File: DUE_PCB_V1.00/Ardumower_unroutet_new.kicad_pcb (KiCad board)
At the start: 2 copper layers, 169.8 x 97 mm, 86 parts, among them J1 9V IN, J10 Sonar_R, J11 Sonar_C, J12 Sonar_L, J13 P_Right, J14 Buzzer, J15 Button, J16 US1, J17 US2, J18 US3, J19 P_Left, J2 I2C0_1, J20 Remote, J21 PCB_2, J22 Ser0, J23 Ser1, J24 Ser2, J25 5V IN, J26 Cutter1, J27 MotorR, J28 MotorL, J29 3.3V IN, J3 I2C0_2, J30 I2C1_2, J31 Ser3, J32 24V In, J33 ReserveD8, J34 ReserveD9, J35 ReserveD49, J36 ReserveA10, J37 RPM_Mow, J38 ODO_Left, J39 ODO_Right, J4 I2C1_1, J40 Motor_Right, J41 Motor_Left, J42 Cutter, J5 Bumper, J6 Drop_Left, J7 Drop_Right, J8 Tilt, J9 Rain, U1 MC33926, U2 MC33926

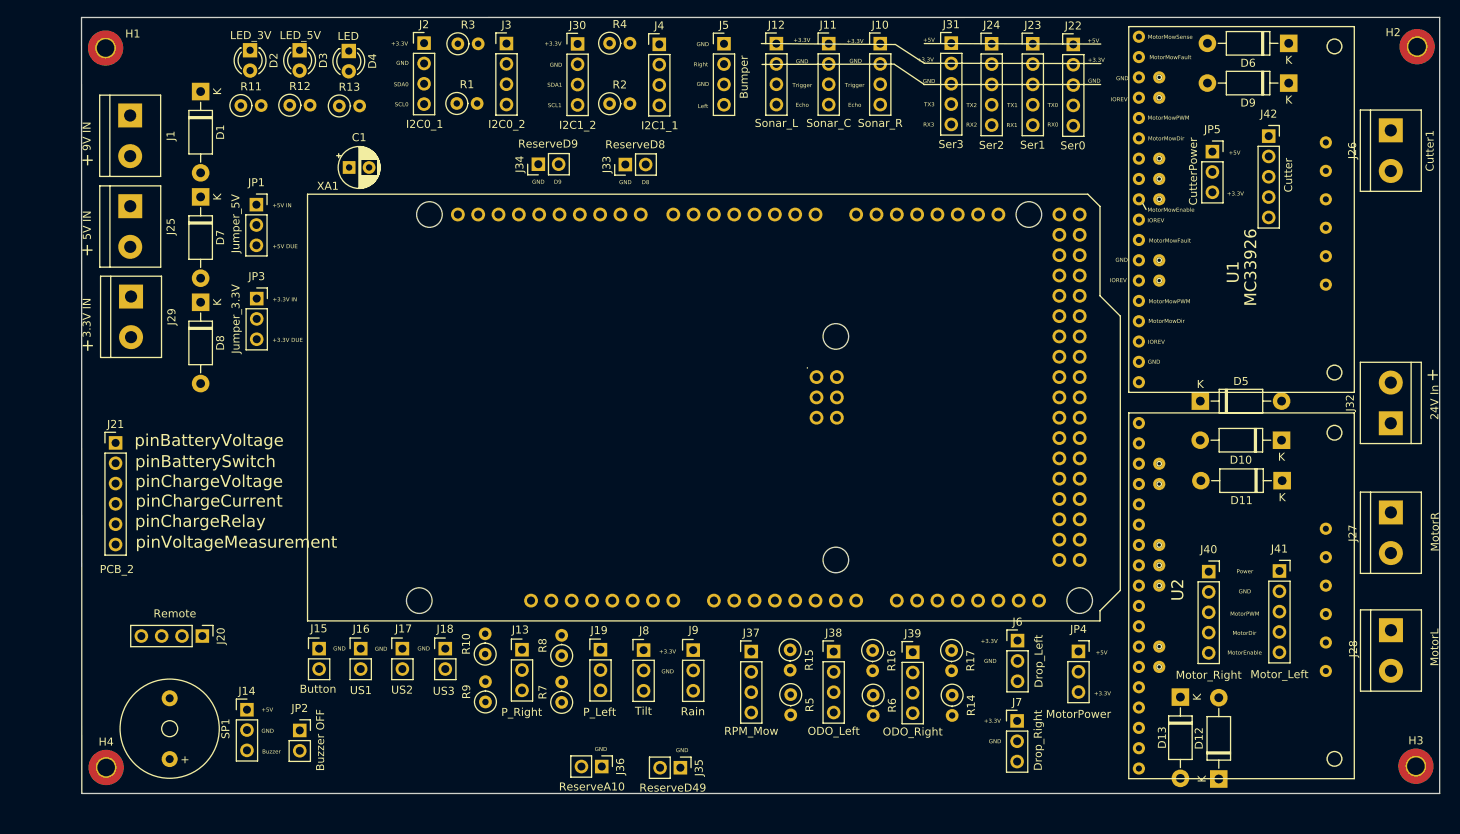
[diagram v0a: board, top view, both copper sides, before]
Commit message: Board Route
Board routed and make Gerber Files
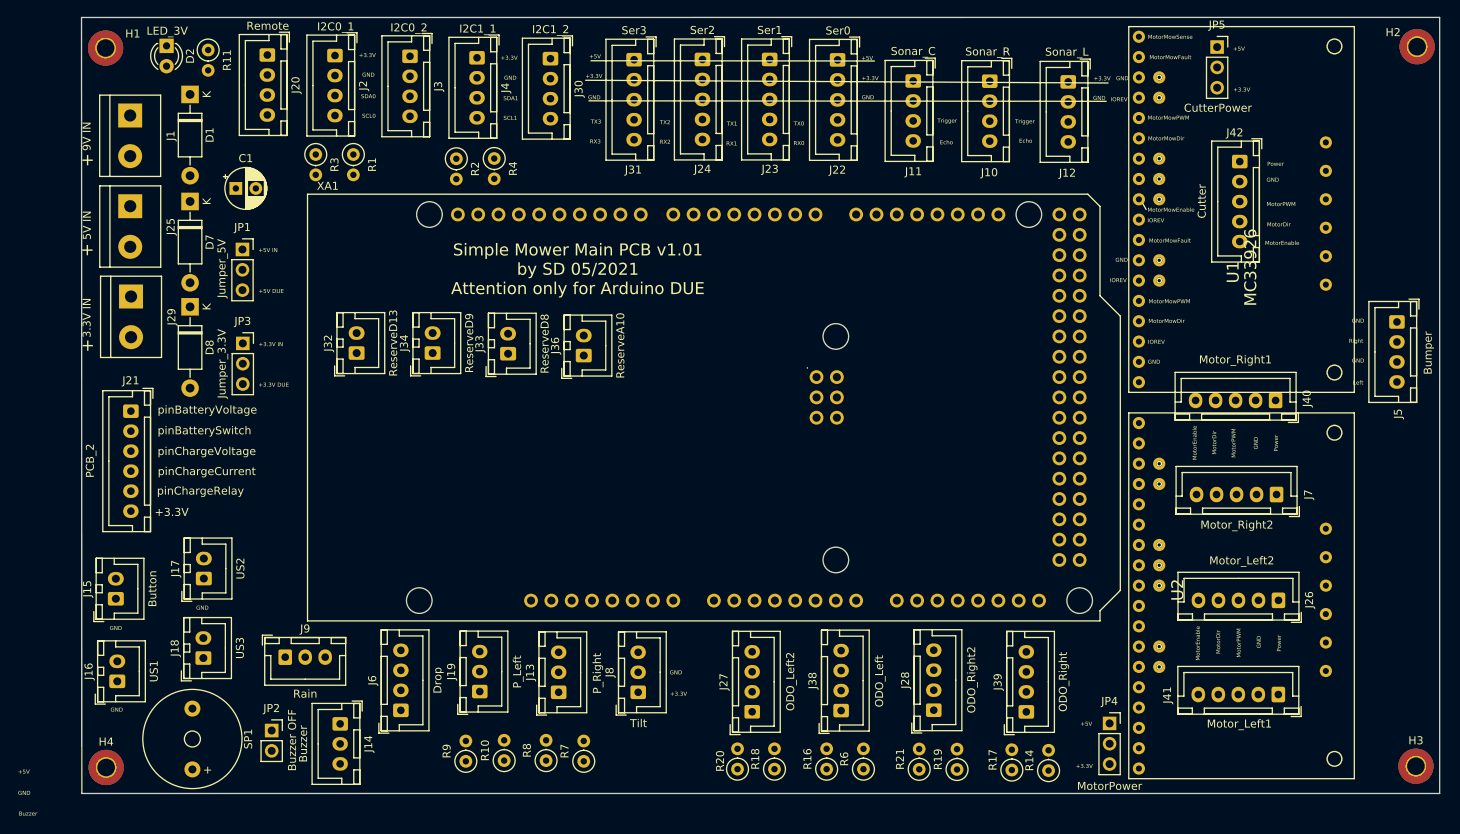
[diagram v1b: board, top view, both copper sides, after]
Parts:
- removed D10, D11, D12, D13, D5, D6, D9: 1N4728A, Diode_THT:D_DO-41_SOD81_P10.16mm_Horizontal
- removed D3: LED_5V, LED_THT:LED_D3.0mm
- removed D4: LED, LED_THT:LED_D3.0mm
- removed J35: ReserveD49, Connector_PinHeader_2.54mm:PinHeader_1x02_P2.54mm_Vertical
- removed J37: RPM_Mow, Connector_PinHeader_2.54mm:PinHeader_1x04_P2.54mm_Vertical
- removed R12: 220, Resistor_THT:R_Axial_DIN0207_L6.3mm_D2.5mm_P2.54mm_Vertical
- removed R13: 100, Resistor_THT:R_Axial_DIN0207_L6.3mm_D2.5mm_P2.54mm_Vertical
- removed R15: 1,5KO, Resistor_THT:R_Axial_DIN0207_L6.3mm_D2.5mm_P2.54mm_Vertical
- removed R5: 1KO, Resistor_THT:R_Axial_DIN0207_L6.3mm_D2.5mm_P2.54mm_Vertical
- added R18: 1KO, Resistor_THT:R_Axial_DIN0207_L6.3mm_D2.5mm_P2.54mm_Vertical, F.Cu at (125.4, 128.6)
- added R19: 1KO, Resistor_THT:R_Axial_DIN0207_L6.3mm_D2.5mm_P2.54mm_Vertical, F.Cu at (148.2, 128.6)
- added R20: 1,5KO, Resistor_THT:R_Axial_DIN0207_L6.3mm_D2.5mm_P2.54mm_Vertical, F.Cu at (120.8, 128.6)
- added R21: 1,5KO, Resistor_THT:R_Axial_DIN0207_L6.3mm_D2.5mm_P2.54mm_Vertical, F.Cu at (143.5, 128.6)
- J10, J11, J12, J2, J20, J3, J30, J38, J39, J4, J5: footprint Connector_PinHeader_2.54mm:PinHeader_1x04_P2.54mm_Vertical -> Connector_JST:JST_XH_B4B-XH-A_1x04_P2.50mm_Vertical
- J13, J14, J19, J8, J9: footprint Connector_PinHeader_2.54mm:PinHeader_1x03_P2.54mm_Vertical -> Connector_JST:JST_XH_B3B-XH-A_1x03_P2.50mm_Vertical
- J15, J16, J17, J18, J33, J34, J36: footprint Connector_PinHeader_2.54mm:PinHeader_1x02_P2.54mm_Vertical -> Connector_JST:JST_XH_B2B-XH-A_1x02_P2.50mm_Vertical
- J21: footprint Connector_PinHeader_2.54mm:PinHeader_1x06_P2.54mm_Vertical -> Connector_JST:JST_XH_B6B-XH-A_1x06_P2.50mm_Vertical
- J22, J23, J24, J31: footprint Connector_PinHeader_2.54mm:PinHeader_1x05_P2.54mm_Vertical -> Connector_JST:JST_XH_B5B-XH-A_1x05_P2.50mm_Vertical
- J26: value Cutter1 -> Motor_Left2; footprint TerminalBlock:TerminalBlock_bornier-2_P5.08mm -> Connector_JST:JST_XH_B5B-XH-A_1x05_P2.50mm_Vertical
- J27: value MotorR -> ODO_Left2; footprint TerminalBlock:TerminalBlock_bornier-2_P5.08mm -> Connector_JST:JST_XH_B4B-XH-A_1x04_P2.50mm_Vertical
- J28: value MotorL -> ODO_Right2; footprint TerminalBlock:TerminalBlock_bornier-2_P5.08mm -> Connector_JST:JST_XH_B4B-XH-A_1x04_P2.50mm_Vertical
- J32: value 24V In -> ReserveD13; footprint TerminalBlock:TerminalBlock_bornier-2_P5.08mm -> Connector_JST:JST_XH_B2B-XH-A_1x02_P2.50mm_Vertical
- J40: value Motor_Right -> Motor_Right1; footprint Connector_PinSocket_2.54mm:PinSocket_1x05_P2.54mm_Vertical -> Connector_JST:JST_XH_B5B-XH-A_1x05_P2.50mm_Vertical
- J41: value Motor_Left -> Motor_Left1; footprint Connector_PinSocket_2.54mm:PinSocket_1x05_P2.54mm_Vertical -> Connector_JST:JST_XH_B5B-XH-A_1x05_P2.50mm_Vertical
- J42: footprint Connector_PinSocket_2.54mm:PinSocket_1x05_P2.54mm_Vertical -> Connector_JST:JST_XH_B5B-XH-A_1x05_P2.50mm_Vertical
- J6: value Drop_Left -> Drop; footprint Connector_PinHeader_2.54mm:PinHeader_1x03_P2.54mm_Vertical -> Connector_JST:JST_XH_B4B-XH-A_1x04_P2.50mm_Vertical
- J7: value Drop_Right -> Motor_Right2; footprint Connector_PinHeader_2.54mm:PinHeader_1x03_P2.54mm_Vertical -> Connector_JST:JST_XH_B5B-XH-A_1x05_P2.50mm_Vertical
- moved J32 129.6 mm to (73.2, 76.6)
- moved J5 91.0 mm to (203.2, 72.7), turned to 270 degrees
- moved J27 83.6 mm to (122.6, 121.4), turned to 90 degrees
- moved J6 77.6 mm to (78.7, 121.2), turned to 90 degrees
- moved J20 73.1 mm to (62.0, 39.3)
- moved J26 60.4 mm to (188.4, 107.5), turned to 180 degrees
- moved J28 58.0 mm to (145.3, 121.2), turned to 90 degrees
- moved J36 51.4 mm to (101.6, 76.9), turned to 90 degrees
- moved J9 51.0 mm to (64.3, 114.6)
- moved J7 43.0 mm to (188.2, 94.2), turned to 180 degrees
- moved J31 39.7 mm to (107.9, 39.9), turned to 270 degrees
- moved J12 36.8 mm to (162.1, 42.7), turned to 270 degrees
- moved J24 36.2 mm to (116.4, 39.9), turned to 270 degrees
- moved J23 32.9 mm to (124.8, 39.9), turned to 270 degrees
- moved J16 30.7 mm to (43.3, 117.6), turned to 90 degrees
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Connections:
- net pinChargeRelay renamed pinChargeEnable
- J21 pad 6: pinVoltageMeasurement -> +3V3
- J26 pad 2: Net-(J26-Pad2) -> GND
- J27 pad 2: Net-(J27-Pad2) -> GND
- J28 pad 2: Net-(J28-Pad2) -> GND
- J32 pad 2: Net-(D5-Pad2) -> pinReserveD13
- J40 pad 1: Net-(J40-Pad1) -> Net-(J26-Pad1)
- J41 pad 1: Net-(J40-Pad1) -> Net-(J26-Pad1)
- J41 pad 5: pinMotorEnable -> pinMotorLeftEnable
- J6 pad 1: +3V3 -> GND
- J6 pad 2: GND -> pinDropLeft
- J6 pad 3: pinDropLeft -> GND
- J7 pad 1: +3V3 -> Net-(J26-Pad1)
- J7 pad 3: pinDropRight -> pinMotorRight2PWM
- JP4 pad 2: Net-(J40-Pad1) -> Net-(J26-Pad1)
- R11 pad 2: +3V3 -> DUE_3.3V
- U1 pad 17: Net-(D9-Pad2) -> pinMotorMowFault
- U1 pad 18: Net-(D6-Pad2) -> pinMotorMowSense
- U1 pad 21: GND -> (no net)
- U1 pad 22: +24V -> (no net)
- U1 pad 23: Net-(J26-Pad2) -> (no net)
- U1 pad 24: Net-(J26-Pad1) -> (no net)
- U1 pad 8: Net-(D9-Pad2) -> pinMotorMowFault
- U1 pad 9: IOREV -> pinMotorMow1Sense
- U2 pad 17: Net-(D11-Pad2) -> pinMotorRightFault
- U2 pad 18: Net-(D10-Pad2) -> pinMotorRightSense
- U2 pad 19: Net-(J28-Pad2) -> (no net)
- U2 pad 20: Net-(J28-Pad1) -> (no net)
- U2 pad 21: GND -> (no net)
- U2 pad 22: +24V -> (no net)
- U2 pad 23: Net-(J27-Pad2) -> (no net)
- U2 pad 24: Net-(J27-Pad1) -> (no net)
- U2 pad 8: Net-(D13-Pad2) -> pinMotorLeftFault
- U2 pad 9: Net-(D12-Pad2) -> pinMotorLeftSense
- XA1 pad A11: pinMotorMowRpm -> (no net)
- XA1 pad A6: (no net) -> pinMotorMow1Sense
- XA1 pad A7: pinVoltageMeasurement -> (no net)
- XA1 pad CANT: (no net) -> pinOdometryRight2
- XA1 pad D13: pinLED -> pinReserveD13
- XA1 pad D40: (no net) -> pinMotorLeft2Dir
- XA1 pad D41: (no net) -> pinMotorRight2Dir
- XA1 pad D42: (no net) -> pinMotorLeft2Enable
- XA1 pad D43: (no net) -> pinMotorRight2Enable
- XA1 pad D49: pinReserveD49 -> pinMotorLeftEnable
- XA1 pad D6: (no net) -> pinMotorLeft2PWM
- XA1 pad D7: (no net) -> pinMotorRight2PWM
- XA1 pad DAC1: (no net) -> pinOdometryLeft2
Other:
- board text added: "Simple Mower Main PCB v1.01 by SD 05/2021 Attention only for Arduino DUE"
- board text removed: "D8"
- board text removed: "D9"
- board text removed: "pinVoltageMeasurement"
